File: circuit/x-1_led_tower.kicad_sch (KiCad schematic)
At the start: 17 parts, among them Q1 PMOS, Q2 NMOS, Q3 PMOS, Q4 NMOS, Q5 PMOS, Q6 NMOS

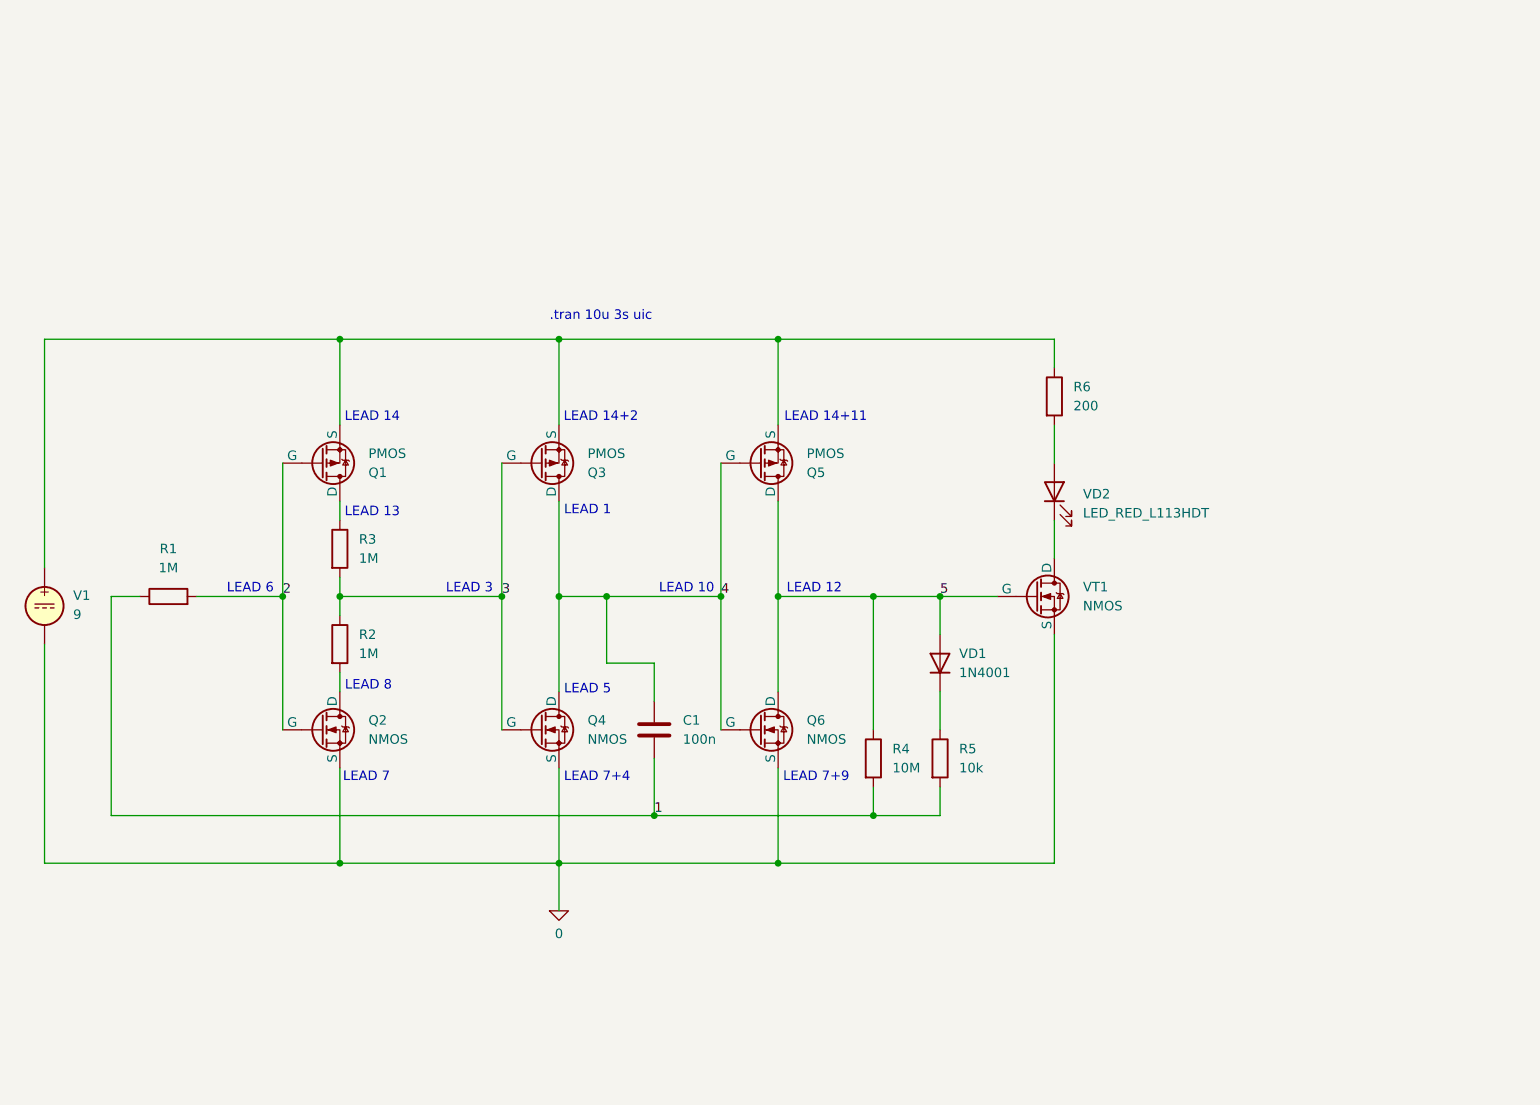
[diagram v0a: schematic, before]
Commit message: add KiCAD circuit
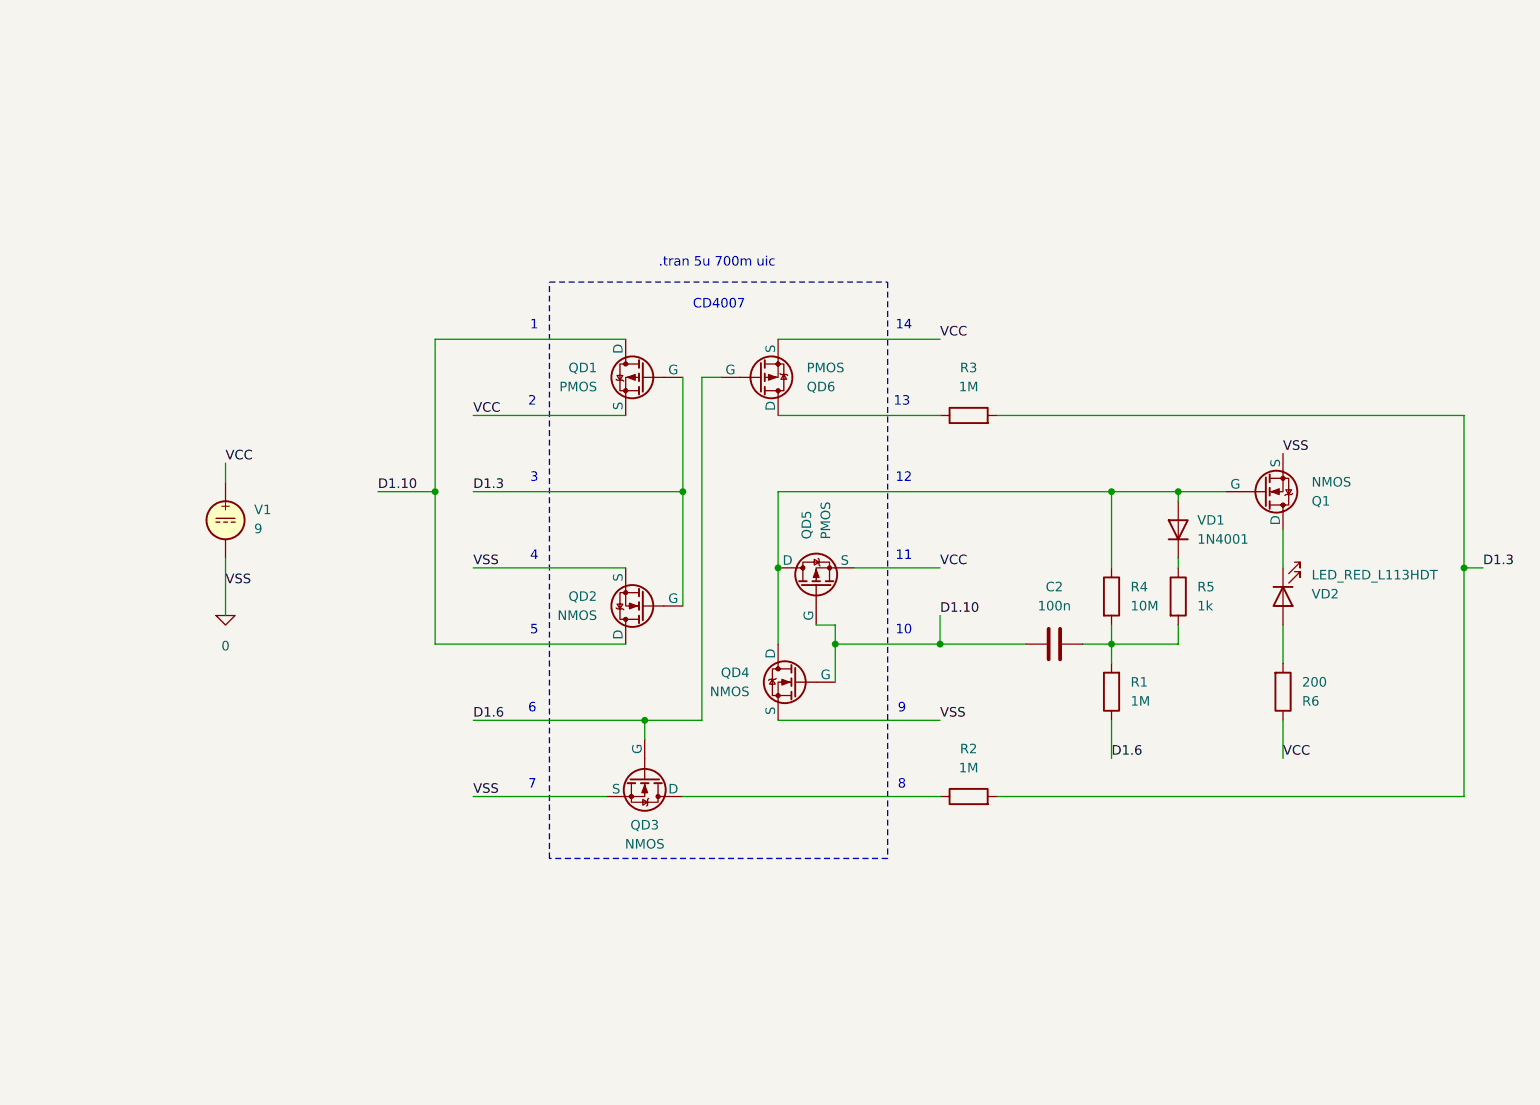
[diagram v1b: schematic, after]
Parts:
- removed C1: 100n, symbol Device:C
- removed Q1, Q3, Q5: PMOS, symbol Simulation_SPICE:PMOS
- removed Q2, Q4, Q6, VT1: NMOS, symbol Simulation_SPICE:NMOS
- added C2: 100n, symbol Device:C
- added Q1, QD2, QD3, QD4: NMOS, symbol Simulation_SPICE:NMOS
- added QD1, QD5, QD6: PMOS, symbol Simulation_SPICE:PMOS
- R5: value 10k -> 1k
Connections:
- net 2 is gone; now on an unnamed net: R1.2
- net 0: now also Q1.3 (S), QD2.3 (S), QD3.3 (S), QD4.3 (S)
- net at VD2.1 (K): now also Q1.1 (D)
- net VCC: now reaches R6.1, V1.1
- net VCC: now also QD1.3 (S), QD5.3 (S), QD6.3 (S)
- net at R3.1: now also QD6.1 (D)
- net D1.3: now reaches R2.2
- net D1.3: now also R3.2, QD1.2 (G), QD2.2 (G)
- net 1: no longer names the net of R4.2, R5.2
- net 1: now also C2.2; no longer R1.1
- net 3: no longer names the net of R2.1
- net 3: now also QD3.1 (D); no longer R3.2
- net 5: no longer names the net of R4.1, VD1.2 (A)
- net 5: now also Q1.2 (G), QD4.1 (D), QD5.1 (D)
- new net D1.10: C2.1, QD1.1 (D), QD2.1 (D), QD4.2 (G), QD5.2 (G)
- new net D1.6: QD3.2 (G), QD6.2 (G), R1.1
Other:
- note added: ".tran 5u 700m uic"
- note added: "1"
- note added: "10"
- note added: "11"
- note added: "12"
- note added: "13"
- note added: "14"
- note added: "2"
- note added: "3"
- note added: "4"
- note added: "5"
- note added: "6"
- note added: "7"
- note added: "8"
- note added: "9"
- note added: "CD4007"
- note removed: ".tran 10u 3s uic"
- note removed: "LEAD 1"
- note removed: "LEAD 10"
- note removed: "LEAD 12"
- note removed: "LEAD 13"
- note removed: "LEAD 14"
- note removed: "LEAD 14+11"
- note removed: "LEAD 14+2"
- note removed: "LEAD 3"
- note removed: "LEAD 5"
- note removed: "LEAD 6"
- note removed: "LEAD 7"
- note removed: "LEAD 7+4"
- note removed: "LEAD 7+9"
- note removed: "LEAD 8"
- moved on the sheet: V1

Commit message: v.5.2 final
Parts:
- added C12, C13, C14, C15: 0.3p, symbol Device:C
- added C2, C3, C4, C5, C6, C7: 100n, symbol Device:C
- renumbered C2 to C1
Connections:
- net 0: now also C2.1, C3.2, C4.1, C5.2
- net VCC: now also C2.2, C3.1, C4.2, C5.1, C6.2, C7.2
- net VD2.A: now reaches R6.2, VD2.2 (A)
- net VD2.A: now also C12.2, C13.1, C14.1, C15.1, C6.1
- net VD2.C: now reaches Q1.1 (D), VD2.1 (K)
- net VD2.C: now also C12.1, C13.2, C14.2, C15.2, C7.1
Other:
- note added: "Frame capacitors"
- moved on the sheet: C1, Q1, QD1, QD2, QD3, QD4, QD5, QD6, R1, R2, R3, R4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
